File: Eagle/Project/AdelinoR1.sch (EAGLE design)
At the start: 59 parts, among them J1 DC-044-A, J2 YELLOW-6P-2.54, J3 YELLOW-8P-2.54, J4 YELLOW-8P-2.54, J5 YELLOW-8P-2.54, Q1 NCE3407A, Q2 CJ2305, U1 ATMEGA32U4-TQFP44, U2 CJT1117-5.0-SOT223, U3 ESP-12F / OPL: 317060163 / SM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, U4 CJT1117-3.3-SOT223, X1 306010049_XTAL_16MHZ-3225_4P

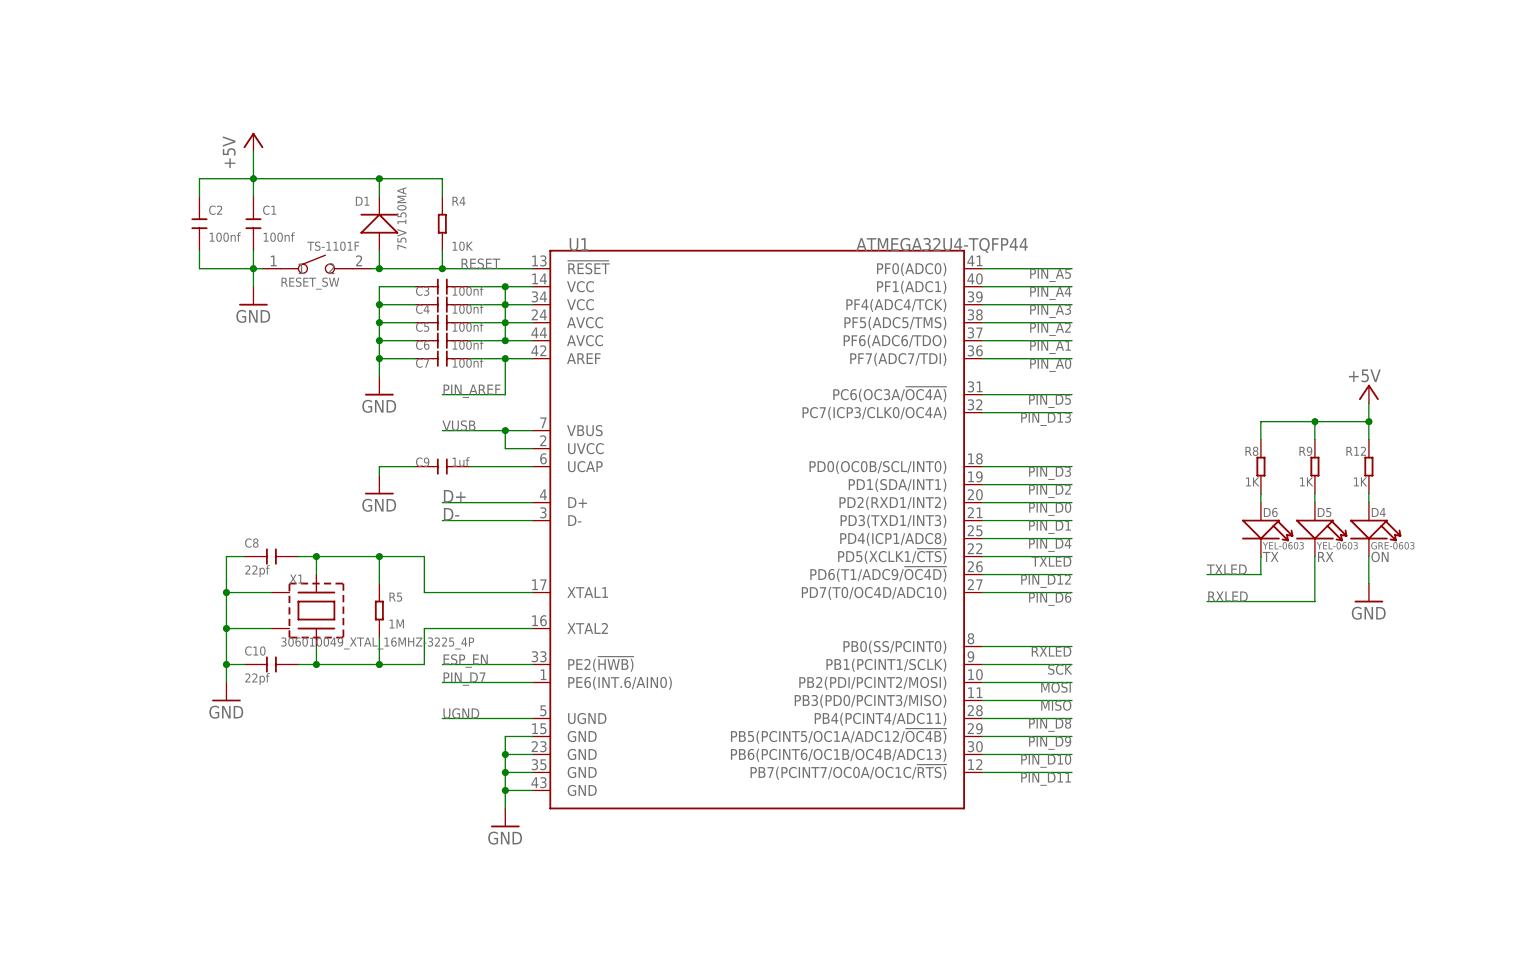
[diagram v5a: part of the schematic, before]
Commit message: Change reset switch to be readable.
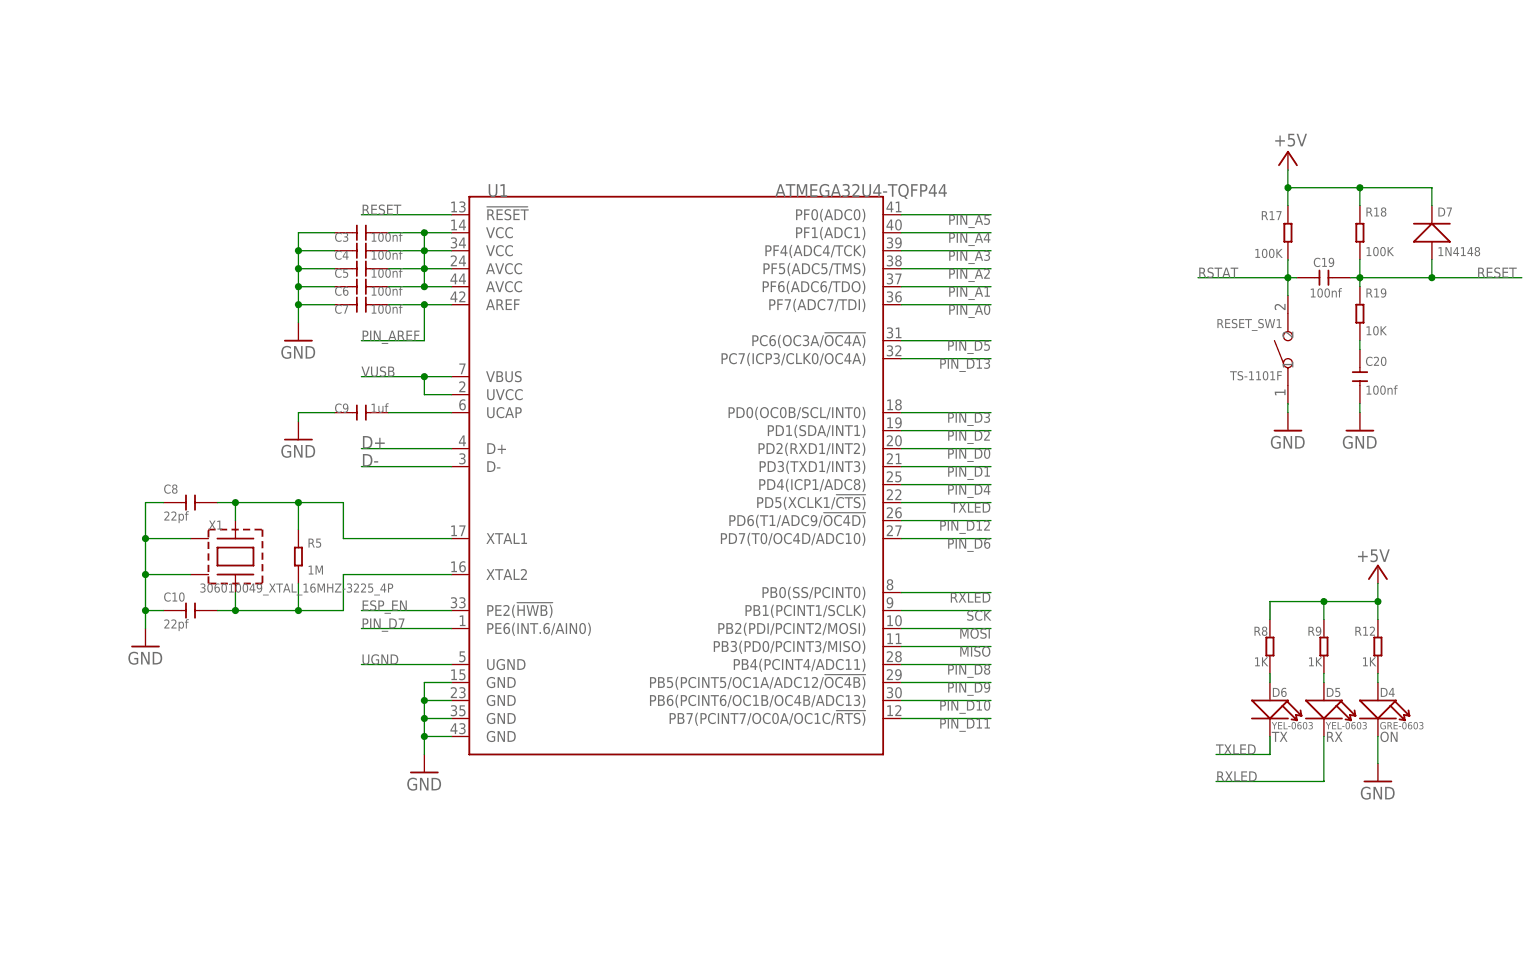
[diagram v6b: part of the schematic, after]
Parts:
- removed C1, C2: 100nf, Seeed-Capacitor:CERAMIC-100NF-25V-10%-X7R(0402)
- removed D1: 75V 150MA, Seeed-Diode:SMD-DIODE-SWITCHING-75V-150MA(D1206)
- removed R4: 10K, Seeed-Resistor:SMD-RES-10K-1%-1/10W(0603)
- removed RESET_SW: TS-1101F, Seeed-Switch:DIP-BUTTON(2P-6.0X3.0X4.3MM)-TS-1101F
- added C19, C20: 100nf, Seeed-Capacitor:CERAMIC-100NF-25V-10%-X7R(0402)
- added D7: 1N4148, Seeed-OPL-2017-01-Diode-james:SMD-DIODE-SWITCH-1N4148(LL-34)
- added R17, R18: 100K, Seeed-Resistor:SMD-RES-100K-1%-1/16W(0402)
- added R19: 10K, Seeed-Resistor:SMD-RES-10K-1%-1/16W(0402)
- added RESET_SW1: TS-1101F, Seeed-Switch:DIP-BUTTON(2P-6.0X3.0X4.3MM)-TS-1101F
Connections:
- new net N$13: C20.1, R19.2
- new net RSTAT: C19.2, R17.2, RESET_SW1.2
- net +5V: now also D7.-, R17.1, R18.2; no longer C1.2, C2.2, D1.-, R4.2
- net GND: now also C20.2, RESET_SW1.1; no longer C1.1, C2.1, RESET_SW.1
- net RESET: now also C19.1, D7.+, R18.1, R19.1; no longer D1.+, R4.1, RESET_SW.2
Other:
- moved on the sheet: C10, C3, C4, C5, C6, C7, C8, C9, D4, D5, D6, R12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

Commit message: Adelino X1 prototype pending revision.
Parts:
- added D1: BLUE-0603, Seeed-LED:SMD-LED-CLEAR-BLUE(0603)
- added R4: 470R, Seeed-Resistor:SMD-RES-470R-5%-1/16W(0402)
- C10, C8: device Seeed-Capacitor:CERAMIC-22PF-50V-5%-NPO(0603) -> Seeed-Capacitor:CERAMIC-22PF-50V-5%-NPO(0402)
- D4: LABEL ON -> PWR
- D5: LABEL RX -> ACT
- D6: LABEL TX -> D13
- D7: value 1N4148 -> 20V-500MA; device Seeed-OPL-2017-01-Diode-james:SMD-DIODE-SWITCH-1N4148(LL-34) -> Seeed-Diode:SMD-DIODE-SCHOTTKY-20V-500MA(SOD-123)P
- R1, R2: device Seeed-Resistor:SMD-RES-22R-5%-1/10W(0603) -> Seeed-Resistor:SMD-RES-22R-1%-1/16W(0402)
- R10, R11, R13, R14, R15, R16: value 1K -> 4.7K; device Seeed-Resistor:SMD-RES-1K-1%-1/10W(0603) -> Seeed-Resistor:SMD-RES-4.7K-5%-1/16W(0402)
- R12, R8, R9: device Seeed-Resistor:SMD-RES-1K-1%-1/10W(0603) -> Seeed-Resistor:SMD-RES-1K-5%-1/16W(0402)
- R3: value 100K 1/10W -> 100K; device Seeed-Resistor:SMD-RES-100K-5%-1/10W(0603) -> Seeed-Resistor:SMD-RES-100K-1%-1/16W(0402)
- R5: device Seeed-Resistor:SMD-RES-1M-1%-1/10W(0603) -> Seeed-Resistor:SMD-RES-1M-1%-1/16W(0402)
- R6: device Seeed-Resistor:SMD-RES-10K-1%-1/10W(0603) -> Seeed-Resistor:SMD-RES-10K-5%-1/(0402)
- R7: value 20K -> 10K; device Seeed-Resistor:SMD-RES-20K-1%-1/10W(0603) -> Seeed-Resistor:SMD-RES-10K-1%-1/16W(0402)
- renumbered RESET_SW1 to RESET_SW
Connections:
- net N$5 renamed XTAL1
- net N$6 renamed XTAL2
- removed net N$15: R11.1, R7.1, U3.GPIO0
- removed net N$19: D5.+, R9.2
- removed net N$20: D6.+, R8.2
- removed net RXLED: D5.-, U1.PB0(SS/PCINT0)
- new net GPIO0: D1.-, R11.1, R7.1, U3.GPIO0
- new net N$12: D1.+, R4.1
- new net N$6: D5.-, R9.1
- new net SS: U1.PB0(SS/PCINT0)
- net +3V3: now also R10.1, R4.2
- net +5V: now also C3.1, C4.1, C5.1, C6.1, D5.+, D6.+, U1.AVCC@1, U1.AVCC@2, U1.VCC@1, U1.VCC@2; no longer R8.1, R9.1
- net ESP_EN: now also R10.2; no longer R10.1, U1.PE2(!HWB)
- net GND: now also RESET_SW.2; no longer C9.1, R10.2, RESET_SW.1, X1.GND1, X1.GND2
- net N$8: now also D6.-, R8.1; no longer C3.1, C4.1, C5.1, C6.1, U1.AVCC@1, U1.AVCC@2, U1.VCC@1, U1.VCC@2
- net PIN_D13: now also R8.2
- net RSTAT: now also RESET_SW.1, U1.PE2(!HWB); no longer RESET_SW.2
- net TXLED: now also R9.2; no longer D6.-
- net UGND: now also C9.1
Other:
- moved on the sheet: D4, D5, D6, R10, R11, R13, R14, R15, R16, R6, R7, R8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

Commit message: Renumbered parts.
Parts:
- removed C19, C20: 100nf, Seeed-Capacitor:CERAMIC-100NF-25V-10%-X7R(0402)
- added C1: 10uf, Seeed-Capacitor:CERAMIC-10UF-25V-10%-X5R(0805)
- added C2: 100nf, Seeed-Capacitor:CERAMIC-100NF-25V-10%-X7R(0402)
- C13, C14, C15, C18: value 10uf -> 100nf; device Seeed-Capacitor:CERAMIC-10UF-25V-10%-X5R(0805) -> Seeed-Capacitor:CERAMIC-100NF-25V-10%-X7R(0402)
- C16: value 100nf -> 1uf; device Seeed-Capacitor:CERAMIC-100NF-25V-10%-X7R(0402) -> Seeed-Capacitor:CERAMIC-1UF-25V-10%-X7R(0805)
- C3, C5: value 100nf -> 10uf; device Seeed-Capacitor:CERAMIC-100NF-25V-10%-X7R(0402) -> Seeed-Capacitor:CERAMIC-10UF-25V-10%-X5R(0805)
- C8: value 22pf -> 10uf; device Seeed-Capacitor:CERAMIC-22PF-50V-5%-NPO(0402) -> Seeed-Capacitor:CERAMIC-10UF-25V-10%-X5R(0805)
- C9: value 1uf -> 22pf; device Seeed-Capacitor:CERAMIC-1UF-25V-10%-X7R(0805) -> Seeed-Capacitor:CERAMIC-22PF-50V-5%-NPO(0402)
- D1: value BLUE-0603 -> 1K 1/10W; device Seeed-LED:SMD-LED-CLEAR-BLUE(0603) -> Seeed-Fuse:SMD-ESD-CG0603MLC-05E; LABEL WIFI -> (none)
- D3: value 1K 1/10W -> BLUE-0603; device Seeed-Fuse:SMD-ESD-CG0603MLC-05E -> Seeed-LED:SMD-LED-CLEAR-BLUE(0603); LABEL (none) -> WIFI
- D4: value GRE-0603 -> YEL-0603; device Seeed-LED:SMD-LED-CLEAR-GREEN(0603) -> Seeed-LED:SMD-LED-CLEAR-YELLOW(0603); LABEL PWR -> D13
- D6: value YEL-0603 -> GRE-0603; device Seeed-LED:SMD-LED-CLEAR-YELLOW(0603) -> Seeed-LED:SMD-LED-CLEAR-GREEN(0603); LABEL D13 -> PWR
- J2: value YELLOW-6P-2.54 -> YELLOW-8P-2.54; device Seeed-Connector:DIP-YELLOW-FEMALE-HEADER-VERT(6P-2.54) -> Seeed-Connector:DIP-YELLOW-FEMALE-HEADER(8P-2.54)
- J3: value YELLOW-8P-2.54 -> YELLOW-6P-2.54; device Seeed-Connector:DIP-YELLOW-FEMALE-HEADER(8P-2.54) -> Seeed-Connector:DIP-YELLOW-FEMALE-HEADER-VERT(6P-2.54)
- R11: value 4.7K -> 10K; device Seeed-Resistor:SMD-RES-4.7K-5%-1/16W(0402) -> Seeed-Resistor:SMD-RES-10K-1%-1/16W(0402)
- R12: value 1K -> 470R; device Seeed-Resistor:SMD-RES-1K-5%-1/16W(0402) -> Seeed-Resistor:SMD-RES-470R-5%-1/16W(0402)
- R14, R16: value 4.7K -> 1K; device Seeed-Resistor:SMD-RES-4.7K-5%-1/16W(0402) -> Seeed-Resistor:SMD-RES-1K-5%-1/16W(0402)
- R15: value 4.7K -> 100K; device Seeed-Resistor:SMD-RES-4.7K-5%-1/16W(0402) -> Seeed-Resistor:SMD-RES-100K-1%-1/16W(0402)
- R18: value 100K -> 10K; device Seeed-Resistor:SMD-RES-100K-1%-1/16W(0402) -> Seeed-Resistor:SMD-RES-10K-1%-1/16W(0402)
- R19: value 10K -> 1K; device Seeed-Resistor:SMD-RES-10K-1%-1/16W(0402) -> Seeed-Resistor:SMD-RES-1K-5%-1/16W(0402)
- R4: value 470R -> 1M; device Seeed-Resistor:SMD-RES-470R-5%-1/16W(0402) -> Seeed-Resistor:SMD-RES-1M-1%-1/16W(0402)
- R5: value 1M -> 10K; device Seeed-Resistor:SMD-RES-1M-1%-1/16W(0402) -> Seeed-Resistor:SMD-RES-10K-1%-1/16W(0402)
- R6: value 10K -> 4.7K; device Seeed-Resistor:SMD-RES-10K-5%-1/(0402) -> Seeed-Resistor:SMD-RES-4.7K-5%-1/16W(0402)
- R7: value 10K -> 4.7K; device Seeed-Resistor:SMD-RES-10K-1%-1/16W(0402) -> Seeed-Resistor:SMD-RES-4.7K-5%-1/16W(0402)
- R8, R9: value 1K -> 4.7K; device Seeed-Resistor:SMD-RES-1K-5%-1/16W(0402) -> Seeed-Resistor:SMD-RES-4.7K-5%-1/16W(0402)
- U1: value ATMEGA32U4-TQFP44 -> CJT1117-5.0-SOT223; device Seeed-IC:MCU-ATMEGA32U4-AU(TQFP44) -> Seeed-IC:PMIC-CJT1117-5.0(SOT223)
- U2: value CJT1117-5.0-SOT223 -> CJT1117-3.3-SOT223; device Seeed-IC:PMIC-CJT1117-5.0(SOT223) -> Seeed-IC:PMIC-CJT1117-3.3(SOT223)
- U4: value CJT1117-3.3-SOT223 -> ATMEGA32U4-TQFP44; device Seeed-IC:PMIC-CJT1117-3.3(SOT223) -> Seeed-IC:MCU-ATMEGA32U4-AU(TQFP44)
- renumbered DIO1 to J8, I2C to J6, ICSP to J7, RESET_SW to SW1
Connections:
- net +3V3: now also C7.2, C8.2, J2.4, R10.2, R11.2, R12.2, R7.1, U2.OUT; no longer C17.2, C18.2, J3.4, R10.1, R16.2, R4.2, R7.2, U4.OUT
- net +5V: now also C11.1, C12.1, C13.1, C14.1, C4.2, C5.2, C6.2, D4.+, J2.2, J2.5, R15.1, R17.2, R19.1, U1.OUT, U2.IN, U4.AVCC@1, U4.AVCC@2, U4.VCC@1, U4.VCC@2; no longer C12.2, C13.2, C16.2, C3.1, C4.1, C5.1, C6.1, D6.+, J3.2, J3.5, R12.1, R17.1, R18.2, U1.AVCC@1, U1.AVCC@2, U1.VCC@1, U1.VCC@2, U2.OUT, U4.IN
- net D+: now also U4.D+; no longer U1.D+
- net D-: now also U4.D-; no longer U1.D-
- net ESP_EN: now also R7.2; no longer R10.2
- net GND: now also C1.1, C11.2, C12.2, C13.2, C14.2, C15.2, C18.2, C2.1, C3.1, C4.1, C5.1, C6.1, C7.1, C9.1, D1.1, D6.-, J2.6, J2.7, J4.7, R5.1, U1.GND, U4.GND@1, U4.GND@2, U4.GND@3, U4.GND@4; no longer C11.1, C12.1, C13.1, C14.1, C15.1, C16.1, C17.1, C18.1, C20.2, C3.2, C4.2, C5.2, C6.2, C7.2, D3.1, D4.-, J3.6, J3.7, J5.7, R6.1, U1.GND@1, U1.GND@2, U1.GND@3, U1.GND@4, U4.GND
- net GPIO0: now also D3.-, R13.1; no longer D1.-, R7.1
- net MISO: now also U4.PB3(PD0/PCINT3/MISO); no longer U1.PB3(PD0/PCINT3/MISO)
- net MOSI: now also R13.2, U4.PB2(PDI/PCINT2/MOSI); no longer R11.2, U1.PB2(PDI/PCINT2/MOSI)
- net N$1: now also D1.2; no longer D2.2
- net N$10: now also C1.2, C2.2, C3.2, U1.IN; no longer C11.2, C14.2, C15.2, U2.IN
- net N$11: now also R10.1; no longer R16.1
- net N$12: now also D3.+, R12.1; no longer D1.+, R4.1
- net N$13: now also C18.1, R18.2; no longer C20.1, R19.2
- net N$14: now also R6.2; no longer R13.2
- net N$17: now also R8.1; no longer R15.1
- net N$18: now also R9.1; no longer R14.1
- net N$2: now also D2.2; no longer D3.2
- net N$4: now also R5.2; no longer R6.2
- net N$5: now also D6.+, R19.2; no longer D4.+, R12.2
- net N$6: now also R16.1; no longer R9.1
- net N$7: now also C16.2, U4.UCAP; no longer C9.2, U1.UCAP
- net N$8: now also D4.-, R14.1; no longer D6.-, R8.1
- net PIN_A0: now also J3.1, U4.PF7(ADC7/TDI); no longer J2.1, U1.PF7(ADC7/TDI)
- net PIN_A1: now also J3.2, U4.PF6(ADC6/TDO); no longer J2.2, U1.PF6(ADC6/TDO)
- net PIN_A2: now also J3.3, U4.PF5(ADC5/TMS); no longer J2.3, U1.PF5(ADC5/TMS)
- net PIN_A3: now also J3.4, U4.PF4(ADC4/TCK); no longer J2.4, U1.PF4(ADC4/TCK)
- net PIN_A4: now also J3.5, U4.PF1(ADC1); no longer J2.5, U1.PF1(ADC1)
- net PIN_A5: now also J3.6, U4.PF0(ADC0); no longer J2.6, U1.PF0(ADC0)
- net PIN_AREF: now also C15.1, J4.8, U4.AREF; no longer C7.1, J5.8, U1.AREF
- net PIN_D0: now also J5.1, R8.2, U4.PD2(RXD1/INT2); no longer J4.1, R15.2, U1.PD2(RXD1/INT2)
- net PIN_D1: now also J5.2, R9.2, U4.PD3(TXD1/INT3); no longer J4.2, R14.2, U1.PD3(TXD1/INT3)
- net PIN_D10: now also J4.3, U4.PB6(PCINT6/OC1B/OC4B/ADC13); no longer J5.3, U1.PB6(PCINT6/OC1B/OC4B/ADC13)
- net PIN_D11: now also J4.4, U4.PB7(PCINT7/OC0A/OC1C/!RTS); no longer J5.4, U1.PB7(PCINT7/OC0A/OC1C/!RTS)
- net PIN_D12: now also J4.5, U4.PD6(T1/ADC9/!OC4D); no longer J5.5, U1.PD6(T1/ADC9/!OC4D)
- net PIN_D13: now also J4.6, R14.2, U4.PC7(ICP3/CLK0/OC4A); no longer J5.6, R8.2, U1.PC7(ICP3/CLK0/OC4A)
- net PIN_D2: now also J5.3, U4.PD1(SDA/INT1); no longer J4.3, U1.PD1(SDA/INT1)
- net PIN_D3: now also J5.4, U4.PD0(OC0B/SCL/INT0); no longer J4.4, U1.PD0(OC0B/SCL/INT0)
- net PIN_D4: now also J5.5, U4.PD4(ICP1/ADC8); no longer J4.5, U1.PD4(ICP1/ADC8)
- net PIN_D5: now also J5.6, U4.PC6(OC3A/!OC4A); no longer J4.6, U1.PC6(OC3A/!OC4A)
- net PIN_D6: now also J5.7, U4.PD7(T0/OC4D/ADC10); no longer J4.7, U1.PD7(T0/OC4D/ADC10)
- net PIN_D7: now also J5.8, U4.PE6(INT.6/AIN0); no longer J4.8, U1.PE6(INT.6/AIN0)
- net PIN_D8: now also J4.1, U4.PB4(PCINT4/ADC11); no longer J5.1, U1.PB4(PCINT4/ADC11)
- net PIN_D9: now also J4.2, U4.PB5(PCINT5/OC1A/ADC12/!OC4B); no longer J5.2, U1.PB5(PCINT5/OC1A/ADC12/!OC4B)
- net RESET: now also C17.1, J2.3, R17.1, U4.!RESET; no longer C19.1, J3.3, R19.1, U1.!RESET
- net RSTAT: now also C17.2, R15.2, U4.PE2(!HWB); no longer C19.2, R17.2, U1.PE2(!HWB)
- net SCK: now also R6.1, U4.PB1(PCINT1/SCLK); no longer R13.1, U1.PB1(PCINT1/SCLK)
- net SS: now also U4.PB0(SS/PCINT0); no longer U1.PB0(SS/PCINT0)
- net TXLED: now also R16.2, U4.PD5(XCLK1/!CTS); no longer R9.2, U1.PD5(XCLK1/!CTS)
- net UGND: now also C16.1, U4.UGND; no longer C9.1, U1.UGND
- net VIN: now also J2.8; no longer J3.8
- net VUSB: now also U4.UVCC, U4.VBUS; no longer U1.UVCC, U1.VBUS
- net XTAL1: now also C9.2, R4.2, U4.XTAL1; no longer C8.2, R5.2, U1.XTAL1
- net XTAL2: now also R4.1, U4.XTAL2; no longer R5.1, U1.XTAL2
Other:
- moved on the sheet: C11, C12, C13, C14, C15, C16, C17, C18, C3, C4, C5, C6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
